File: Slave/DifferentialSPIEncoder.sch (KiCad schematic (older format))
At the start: 26 parts, among them J1 debug, J2 8P8C_Shielded, U1 TLV71333PDBV, U2 AS5048A, U3 MAX485E, U4 MAX485E, U5 MAX485E

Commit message: converted to +5v only
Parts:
- removed C1: 10nF, Capacitor_SMD:C_0402_1005Metric, symbol Device:C_Small
- removed C2: 100nF, Capacitor_SMD:C_0402_1005Metric, symbol Device:C_Small
- removed J1: debug, Connector_PinSocket_2.54mm:PinSocket_2x03_P2.54mm_Vertical, symbol Connector_Generic:Conn_02x03_Counter_Clockwise
- removed U1: TLV71333PDBV, Package_TO_SOT_SMD:SOT-23-5, symbol Regulator_Linear:TLV71333PDBV
- added C1: 10uF, Capacitor_SMD:C_0603_1608Metric, symbol Device:C
- added J1: Conn_01x05_Male, Connector_PinHeader_2.54mm:PinHeader_1x05_P2.54mm_Vertical, symbol Connector:Conn_01x05_Male
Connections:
- net labels added: V3cap
- net labels removed: +3.3V, MOSI
- wire segments 124 -> 113
- no-connect marks 4 -> 5
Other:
- moved on the sheet: C3, C4, C5, C6, C7, C8, C9, J2, R1, R10, R2, R3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

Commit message: Shame. Shame. Shame.
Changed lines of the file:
@@
 Wire Wire Line
 	3910 3360 3860 3360
-Text GLabel 3020 3315 2    50   BiDi ~ 0
+Text GLabel 3020 3315 2    50   Input ~ 0
 V3cap
 Connection ~ 1840 925
@@
 Wire Wire Line
 	1650 3060 1650 3020
-Text GLabel 1650 3020 1    50   BiDi ~ 0
+Text GLabel 1650 3020 1    50   Output ~ 0
 V3cap
 $Comp
@@
 	2500 3395 2500 3410
 $Comp
-L power:+5V #PWR?
+L power:+5V #PWR0108
 U 1 1 5DAC799E
 P 1750 3020
-F 0 "#PWR?" H 1750 2870 50  0001 C CNN
+F 0 "#PWR0108" H 1750 2870 50  0001 C CNN
 F 1 "+5V" H 1765 3193 50  0000 C CNN
 F 2 "" H 1750 3020 50  0001 C CNN
@@
 	1    0    0    -1
 $EndComp
+$Comp
+L power:+5V #PWR0109
+U 1 1 5E22FEAE
+P 3500 4135
+F 0 "#PWR0109" H 3500 3985 50  0001 C CNN
+F 1 "+5V" H 3515 4308 50  0000 C CNN
+F 2 "" H 3500 4135 50  0001 C CNN
+F 3 "" H 3500 4135 50  0001 C CNN
+	1    3500 4135
+	1    0    0    -1
+$EndComp
+$Comp
+L power:GND #PWR0110
+U 1 1 5E233C39
+P 3500 4455
+F 0 "#PWR0110" H 3500 4205 50  0001 C CNN
+F 1 "GND" H 3505 4282 50  0000 C CNN
+F 2 "" H 3500 4455 50  0001 C CNN
+F 3 "" H 3500 4455 50  0001 C CNN
+	1    3500 4455
+	-1   0    0    -1
+$EndComp
+$Comp
+L power:PWR_FLAG #FLG0101
+U 1 1 5E237BCC
+P 3800 4135
+F 0 "#FLG0101" H 3800 4210 50  0001 C CNN
+F 1 "PWR_FLAG" H 3800 4308 50  0000 C CNN
+F 2 "" H 3800 4135 50  0001 C CNN
+F 3 "~" H 3800 4135 50  0001 C CNN
+	1    3800 4135
+	1    0    0    -1
+$EndComp
+Wire Wire Line
+	3500 4135 3500 4215
+Wire Wire Line
+	3500 4215 3800 4215
+Wire Wire Line
+	3800 4215 3800 4135
+$Comp
+L power:PWR_FLAG #FLG0102
+U 1 1 5E23CAF5
+P 3800 4455
+F 0 "#FLG0102" H 3800 4530 50  0001 C CNN
+F 1 "PWR_FLAG" H 3800 4628 50  0000 C CNN
+F 2 "" H 3800 4455 50  0001 C CNN
+F 3 "~" H 3800 4455 50  0001 C CNN
+	1    3800 4455
+	1    0    0    -1
+$EndComp
+Wire Wire Line
+	3500 4455 3800 4455
+$Comp
+L power:PWR_FLAG #FLG0103
+U 1 1 5E251298
+P 2980 3265
+F 0 "#FLG0103" H 2980 3340 50  0001 C CNN
+F 1 "PWR_FLAG" H 2980 3438 50  0000 C CNN
+F 2 "" H 2980 3265 50  0001 C CNN
+F 3 "~" H 2980 3265 50  0001 C CNN
+	1    2980 3265
+	1    0    0    -1
+$EndComp
+Wire Wire Line
+	2980 3265 2980 3315
+Connection ~ 2980 3315
 $EndSCHEMATC

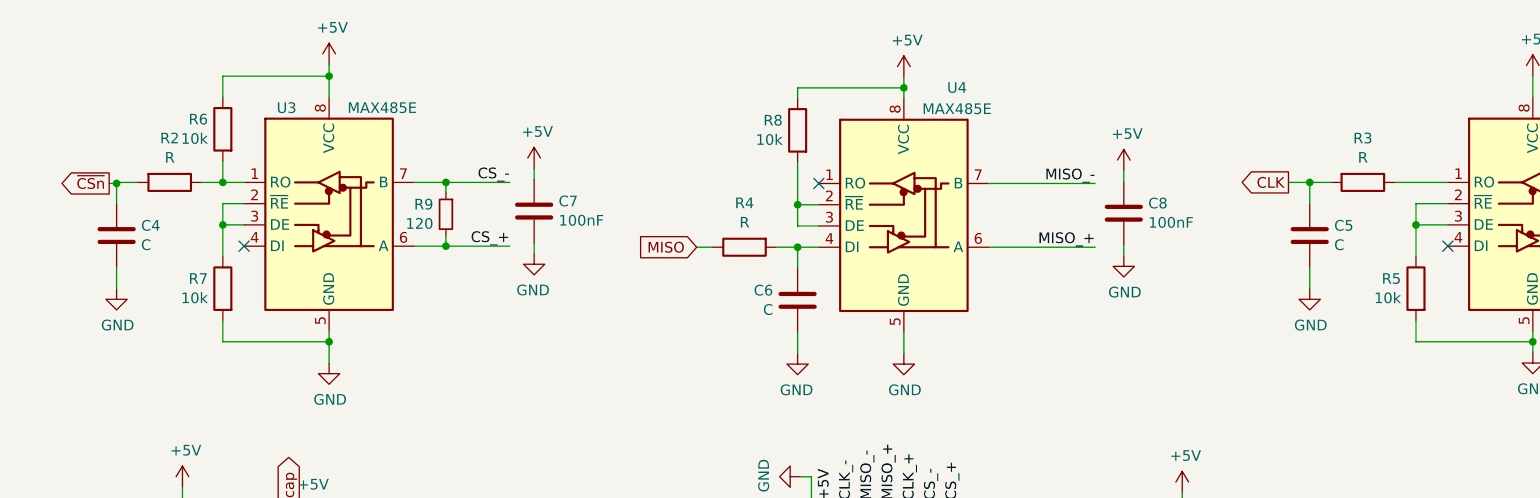
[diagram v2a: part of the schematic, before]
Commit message: Added values for LPFs
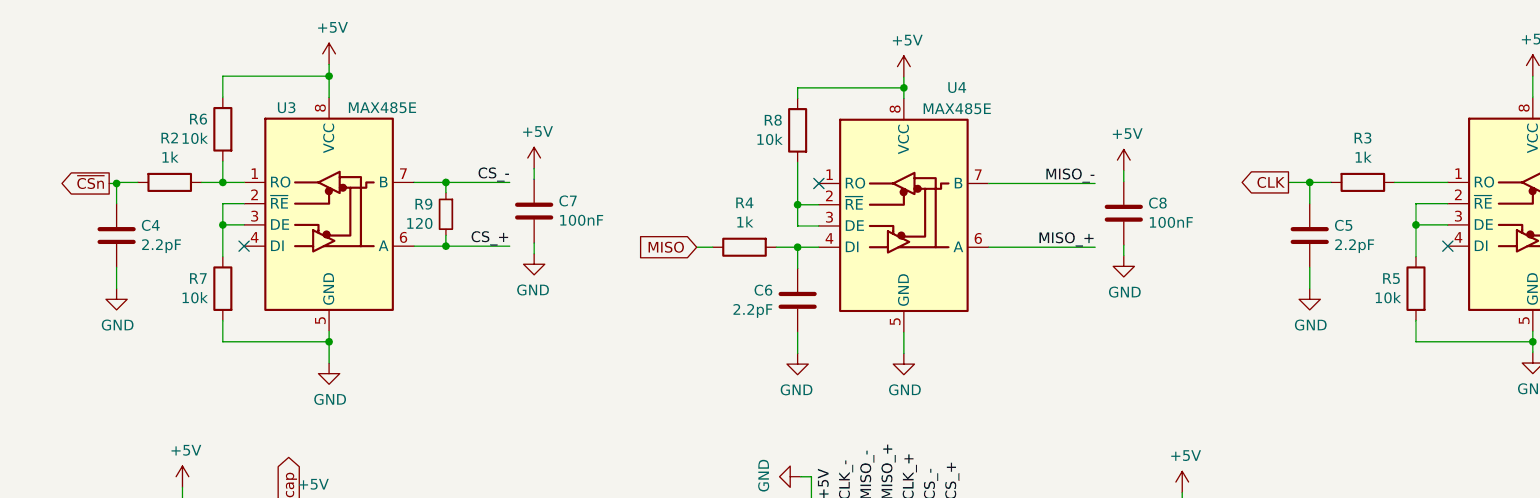
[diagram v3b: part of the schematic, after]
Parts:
- C4, C5, C6: value C -> 2.2pF
- R2, R3, R4: value R -> 1k
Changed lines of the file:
@@
 Sheet 1 1
 Title "SPI DIfferential Encoder"
-Date "2019-05-31"
-Rev "2"
+Date "2019-11-06"
+Rev "3"
 Comp "Wetmelon Enterprises"
 Comment1 ""
@@
 P 1090 1425
 F 0 "R2" V 883 1425 50  0000 C CNN
-F 1 "R" V 974 1425 50  0000 C CNN
+F 1 "1k" V 974 1425 50  0000 C CNN
 F 2 "Resistor_SMD:R_0402_1005Metric" V 1020 1425 50  0001 C CNN
 F 3 "~" H 1090 1425 50  0001 C CNN
@@
 P 6455 1675
 F 0 "C5" H 6570 1721 50  0000 L CNN
-F 1 "C" H 6570 1630 50  0000 L CNN
+F 1 "2.2pF" H 6570 1630 50  0000 L CNN
 F 2 "Capacitor_SMD:C_0402_1005Metric" H 6493 1525 50  0001 C CNN
 F 3 "~" H 6455 1675 50  0001 C CNN
@@
 P 6705 1425
 F 0 "R3" V 6498 1425 50  0000 C CNN
-F 1 "R" V 6589 1425 50  0000 C CNN
+F 1 "1k" V 6589 1425 50  0000 C CNN
 F 2 "Resistor_SMD:R_0402_1005Metric" V 6635 1425 50  0001 C CNN
 F 3 "~" H 6705 1425 50  0001 C CNN
@@
 P 4045 1980
 F 0 "C6" H 4160 2026 50  0000 L CNN
-F 1 "C" H 4160 1935 50  0000 L CNN
+F 1 "2.2pF" H 4160 1935 50  0000 L CNN
 F 2 "Capacitor_SMD:C_0402_1005Metric" H 4083 1830 50  0001 C CNN
 F 3 "~" H 4045 1980 50  0001 C CNN
@@
 P 3795 1730
 F 0 "R4" V 3588 1730 50  0000 C CNN
-F 1 "R" V 3679 1730 50  0000 C CNN
+F 1 "1k" V 3679 1730 50  0000 C CNN
 F 2 "Resistor_SMD:R_0402_1005Metric" V 3725 1730 50  0001 C CNN
 F 3 "~" H 3795 1730 50  0001 C CNN
@@
 P 840 1675
 F 0 "C4" H 955 1721 50  0000 L CNN
-F 1 "C" H 955 1630 50  0000 L CNN
+F 1 "2.2pF" H 955 1630 50  0000 L CNN
 F 2 "Capacitor_SMD:C_0402_1005Metric" H 878 1525 50  0001 C CNN
 F 3 "~" H 840 1675 50  0001 C CNN

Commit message: add BOM for parts
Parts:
- C1: MANUFACTURER (none) -> KEMET; MFN (none) -> C0603C106M8PACTU
- C3, C7, C8, C9: MANUFACTURER (none) -> KEMET; MFN (none) -> C0402C104K8PAC7411
- C4, C5, C6: MANUFACTURER (none) -> KEMET; MFN (none) -> C0402C229C8GACTU
- R1, R5, R6, R7, R8: MANUFACTURER (none) -> Yageo; MFN (none) -> RT0402DRE0710KL
- R10, R9: MANUFACTURER (none) -> Yageo; MFN (none) -> RC0402JR-07120RL
- R2, R3, R4: MANUFACTURER (none) -> Yageo; MFN (none) -> AA0402FR-071KL
- U2: MANUFACTURER (none) -> ams; MFN (none) -> AS5048A-HTSP-500
- U3, U4, U5: MFN (none) -> MAX485ESA+

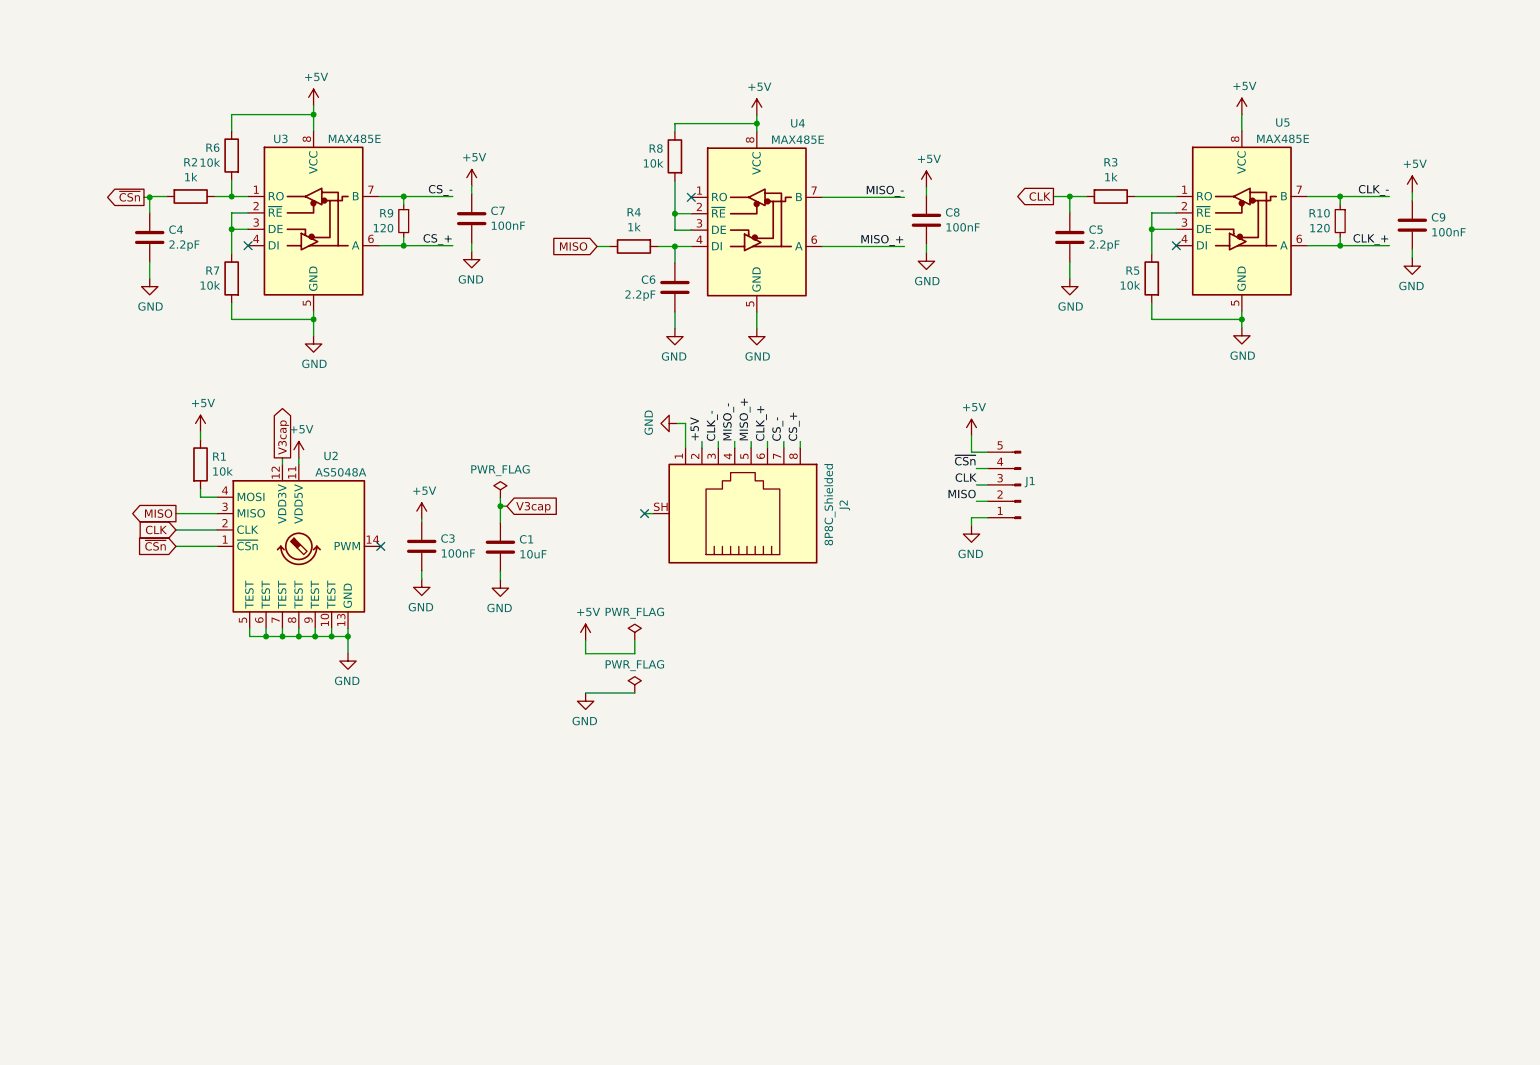
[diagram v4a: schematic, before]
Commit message: Update slave schematic with changes from #2
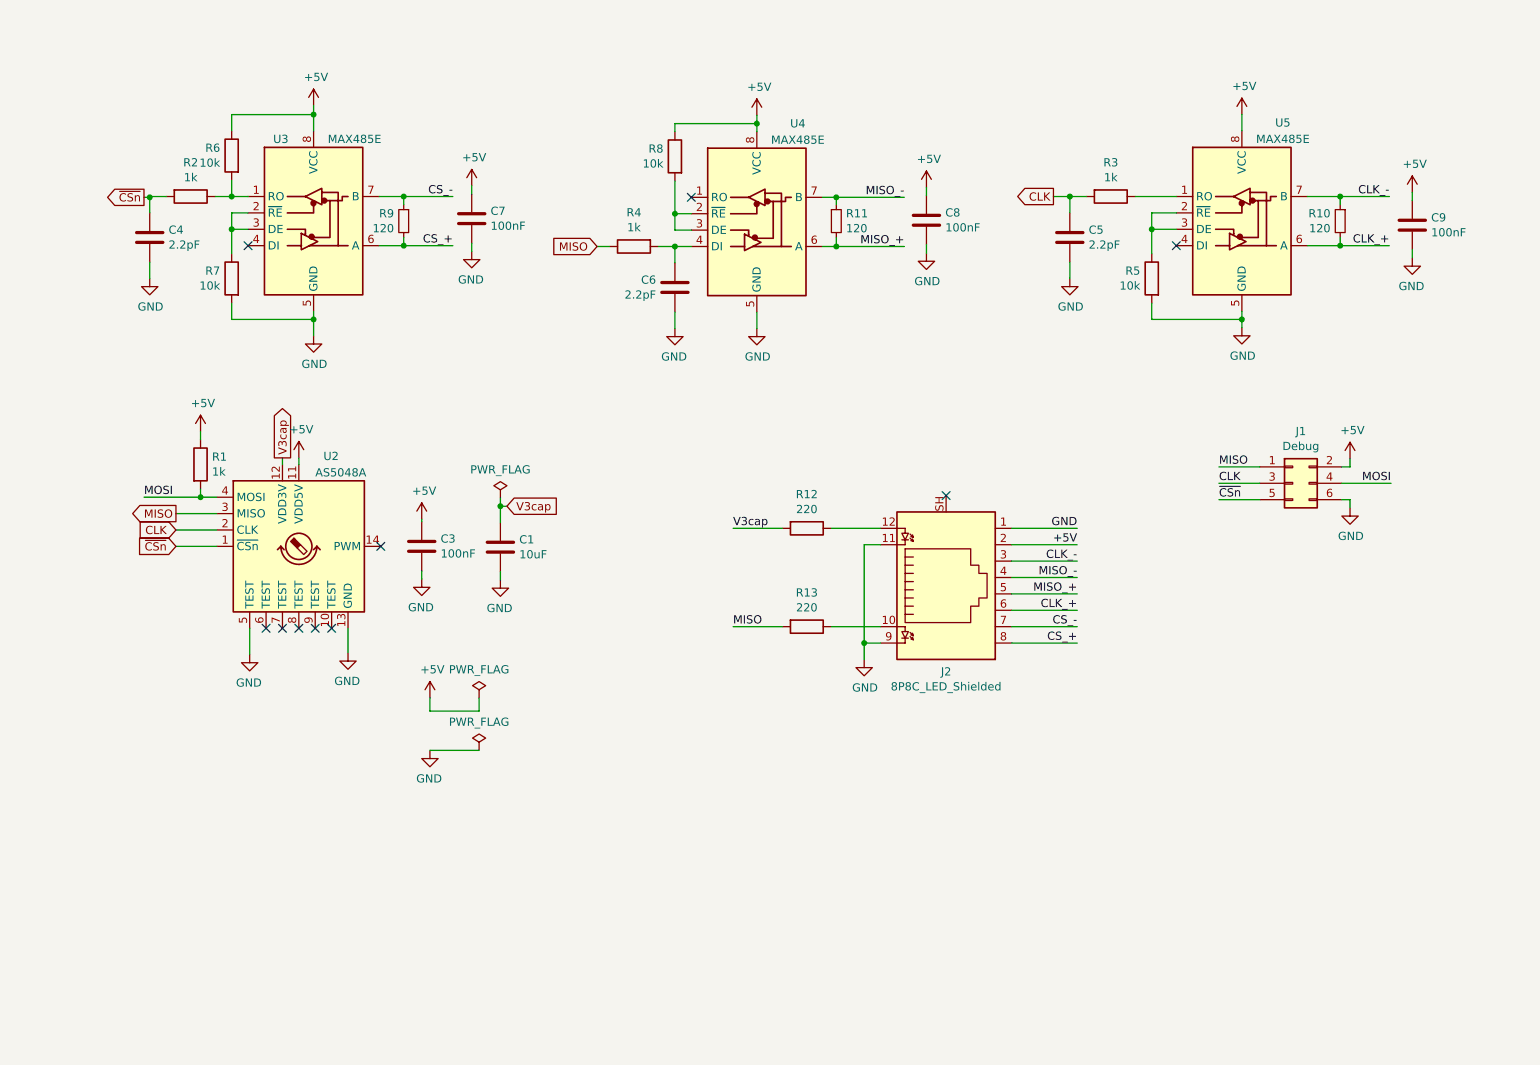
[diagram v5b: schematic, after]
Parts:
- removed J1: Conn_01x05_Male, Connector_PinHeader_2.54mm:PinHeader_1x05_P2.54mm_Vertical, symbol Connector:Conn_01x05_Male
- removed J2: 8P8C_Shielded, Connector_RJ:RJ45_Amphenol_RJHSE5380, symbol Connector:8P8C_Shielded
- added J1: Debug, Connector_PinHeader_2.54mm:PinHeader_2x03_P2.54mm_Vertical, symbol Connector_Generic:Conn_02x03_Odd_Even
- added J2: 8P8C_LED_Shielded, Connector_RJ:RJ45_Amphenol_RJHSE538X, symbol Connector:8P8C_LED_Shielded
- added R11: 120, Resistor_SMD:R_0402_1005Metric, symbol Device:R_Small
- added R12, R13: 220, Resistor_SMD:R_0402_1005Metric, symbol Device:R
- R1: value 10k -> 1k
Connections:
- net +5V: now also J1.2 (Pin_2), J2.2
- net CLK: now also J1.3 (Pin_3)
- net CLK_+: now also J2.6
- net CLK_-: now also J2.3
- net CS_+: now also J2.8
- net CS_-: now also J2.7
- net GND: now also J1.6 (Pin_6), J2.1, J2.11, J2.9; no longer U2.10 (TEST), U2.6 (TEST), U2.7 (TEST), U2.8 (TEST), U2.9 (TEST)
- net MISO: now also J1.1 (Pin_1), R13.2
- net MISO_+: now also J2.5, R11.2
- net MISO_-: now also J2.4, R11.1
- net V3cap: now also R12.2
- net ~CSn: now also J1.5 (Pin_5)
- net MOSI: now reaches R1.2, U2.4 (MOSI)
- net MOSI: now also J1.4 (Pin_4)
- new net: J2.10, R13.1
- new net: J2.12, R12.1
- no-connect marks 5 -> 10

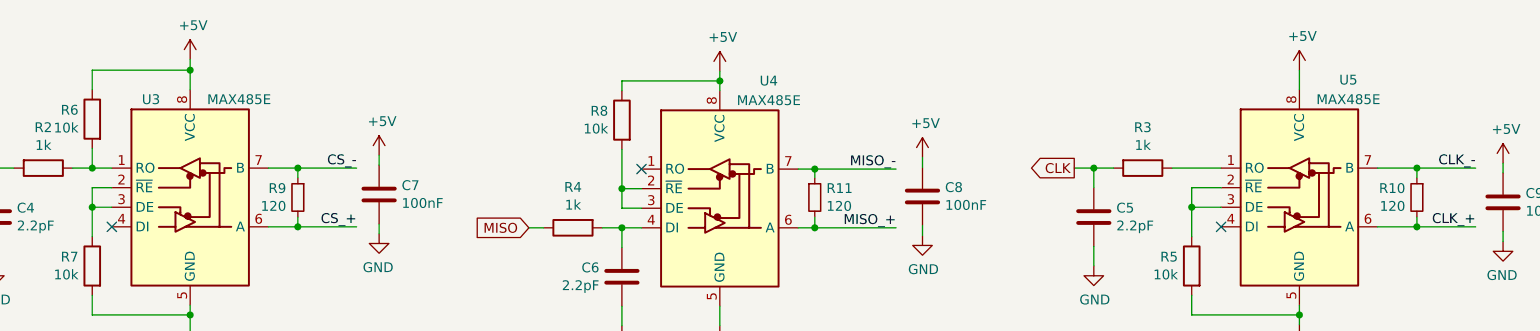
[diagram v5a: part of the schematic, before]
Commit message: Replace MAX485E with SN65HVD06D for 10mbps signaling
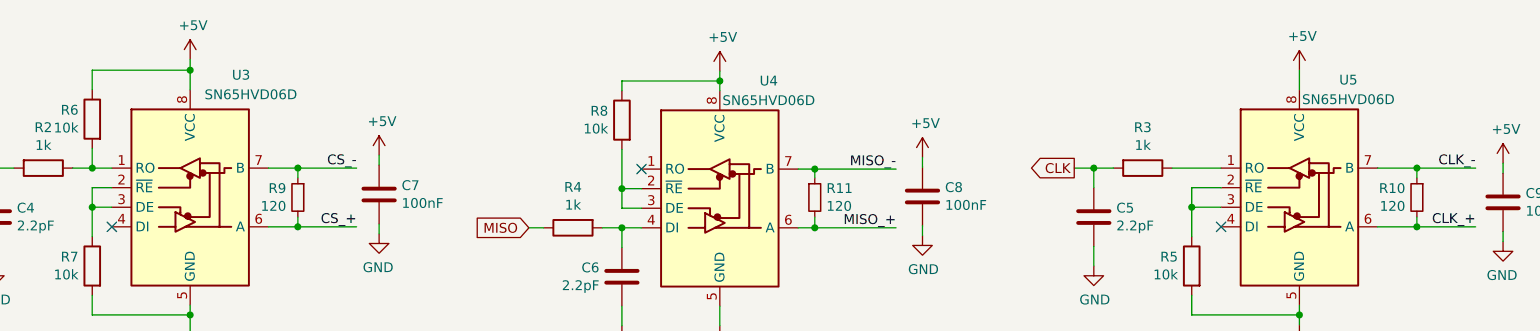
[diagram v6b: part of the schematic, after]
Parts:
- U3, U4, U5: value MAX485E -> SN65HVD06D
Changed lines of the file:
@@
 U 1 1 5CF18800
 P 1840 1525
-F 0 "U3" H 1640 1975 50  0000 C CNN
-F 1 "MAX485E" H 2090 1975 50  0000 C CNN
+F 0 "U3" H 2100 2100 50  0000 C CNN
+F 1 "SN65HVD06D" H 2150 2000 50  0000 C CNN
 F 2 "Package_SO:SOIC-8_3.9x4.9mm_P1.27mm" H 1840 825 50  0001 C CNN
 F 3 "https://www.mouser.com/ProductDetail/Maxim-Integrated/MAX485ESA%2b?qs=sGAEpiMZZMuXae9YOZoWd9EBnNihOkMOJLDcRh71%2FZA%3D" H 1840 1575 50  0001 C CNN
@@
 P 4545 1530
 F 0 "U4" H 4795 2080 50  0000 C CNN
-F 1 "MAX485E" H 4795 1980 50  0000 C CNN
+F 1 "SN65HVD06D" H 4795 1980 50  0000 C CNN
 F 2 "Package_SO:SOIC-8_3.9x4.9mm_P1.27mm" H 4545 830 50  0001 C CNN
 F 3 "https://www.mouser.com/ProductDetail/Maxim-Integrated/MAX485ESA%2b?qs=sGAEpiMZZMuXae9YOZoWd9EBnNihOkMOJLDcRh71%2FZA%3D" H 4545 1580 50  0001 C CNN
@@
 P 7505 1525
 F 0 "U5" H 7755 2075 50  0000 C CNN
-F 1 "MAX485E" H 7755 1975 50  0000 C CNN
+F 1 "SN65HVD06D" H 7755 1975 50  0000 C CNN
 F 2 "Package_SO:SOIC-8_3.9x4.9mm_P1.27mm" H 7505 825 50  0001 C CNN
 F 3 "https://www.mouser.com/ProductDetail/Maxim-Integrated/MAX485ESA%2b?qs=sGAEpiMZZMuXae9YOZoWd9EBnNihOkMOJLDcRh71%2FZA%3D" H 7505 1575 50  0001 C CNN

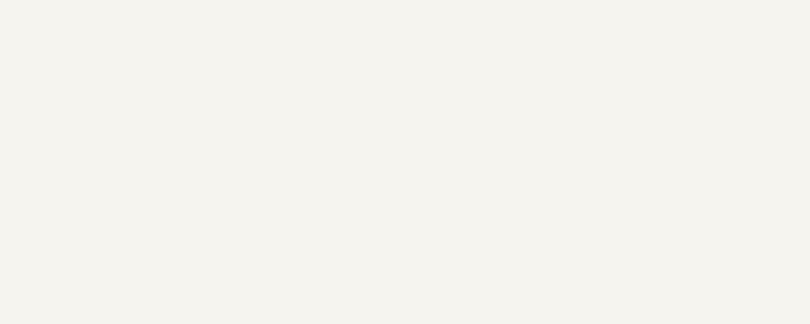
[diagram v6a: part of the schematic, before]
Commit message: Fit slave to AMT102 footprint
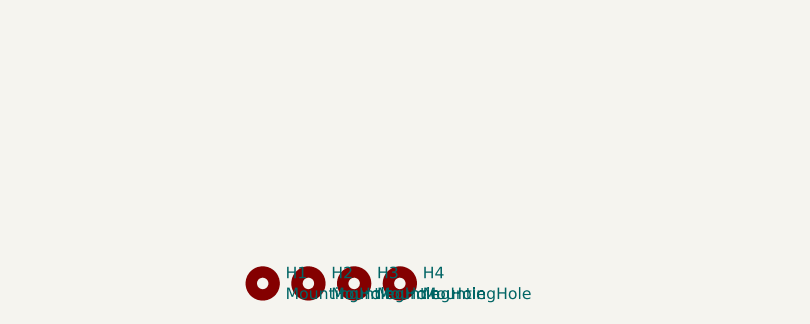
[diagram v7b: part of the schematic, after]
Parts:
- added H1, H2, H3, H4: MountingHole, MountingHole:MountingHole_3.2mm_M3, symbol Mechanical:MountingHole
- J1: footprint Connector_PinHeader_2.54mm:PinHeader_2x03_P2.54mm_Vertical -> Connector_PinHeader_2.54mm:PinHeader_1x06_P2.54mm_Vertical
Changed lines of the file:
@@
 F 0 "J1" H 7865 3492 50  0000 C CNN
 F 1 "Debug" H 7865 3401 50  0000 C CNN
-F 2 "Connector_PinHeader_2.54mm:PinHeader_2x03_P2.54mm_Vertical" H 7815 3175 50  0001 C CNN
+F 2 "Connector_PinHeader_2.54mm:PinHeader_1x06_P2.54mm_Vertical" H 7815 3175 50  0001 C CNN
 F 3 "~" H 7815 3175 50  0001 C CNN
 	1    7815 3175
 	1    0    0    -1
 $EndComp
+$Comp
+L Mechanical:MountingHole H1
+U 1 1 5DE5C6FB
+P 6400 6550
+F 0 "H1" H 6500 6596 50  0000 L CNN
+F 1 "MountingHole" H 6500 6505 50  0000 L CNN
+F 2 "MountingHole:MountingHole_3.2mm_M3" H 6400 6550 50  0001 C CNN
+F 3 "~" H 6400 6550 50  0001 C CNN
+	1    6400 6550
+	1    0    0    -1
+$EndComp
+$Comp
+L Mechanical:MountingHole H2
+U 1 1 5DE5CD83
+P 6600 6550
+F 0 "H2" H 6700 6596 50  0000 L CNN
+F 1 "MountingHole" H 6700 6505 50  0000 L CNN
+F 2 "MountingHole:MountingHole_3.2mm_M3" H 6600 6550 50  0001 C CNN
+F 3 "~" H 6600 6550 50  0001 C CNN
+	1    6600 6550
+	1    0    0    -1
+$EndComp
+$Comp
+L Mechanical:MountingHole H3
+U 1 1 5DE5CFA6
+P 6800 6550
+F 0 "H3" H 6900 6596 50  0000 L CNN
+F 1 "MountingHole" H 6900 6505 50  0000 L CNN
+F 2 "MountingHole:MountingHole_3.2mm_M3" H 6800 6550 50  0001 C CNN
+F 3 "~" H 6800 6550 50  0001 C CNN
+	1    6800 6550
+	1    0    0    -1
+$EndComp
+$Comp
+L Mechanical:MountingHole H4
+U 1 1 5DE5D570
+P 7000 6550
+F 0 "H4" H 7100 6596 50  0000 L CNN
+F 1 "MountingHole" H 7100 6505 50  0000 L CNN
+F 2 "MountingHole:MountingHole_3.2mm_M3" H 7000 6550 50  0001 C CNN
+F 3 "~" H 7000 6550 50  0001 C CNN
+	1    7000 6550
+	1    0    0    -1
+$EndComp
